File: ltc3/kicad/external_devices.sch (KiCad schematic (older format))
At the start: 68 parts, among them IC701 TLP3542, IC702 TLP3542, IC703 TLP3542, IC704 TLP3542, P701 CONN_EXT_PWR_1, P702 CONN_EXT_PWR_2, P703 CONN_EXT_PWR_3, P704 CONN_EXT_PWR_4, Q701 PMV45EN, Q702 PMV45EN, Q703 PMV45EN, Q704 PMV45EN

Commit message: LTC3: Converted hierarchical power pins to global power nodes.
This eliminates the need to manually route power from one top-level
sheet to another.
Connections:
- net VCC_12V renamed +12V
- net VCC_5V renamed +5V
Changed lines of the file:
@@
 LIBS:switches
 LIBS:CD74HC14
+LIBS:power_nodes
 LIBS:Launch_Tower_Computer_III-cache
 EELAYER 25 0
@@
 $Descr B 17000 11000
 encoding utf-8
-Sheet 6 7
+Sheet 5 7
 Title "LTC3 External Device Power"
 Date "2015-11-20"
@@
 	1    0    0    -1
 $EndComp
-Text HLabel 2650 1350 1    60   Input ~ 0
-VCC_12V
 $Comp
 L THERMISTOR PTC701
@@
 Wire Wire Line
 	1150 3000 1150 2850
-Text HLabel 1600 1600 1    60   Input ~ 0
-VCC_5V
 Wire Wire Line
 	2650 1350 2650 1550
@@
 	1    0    0    -1
 $EndComp
-Text HLabel 6850 1250 1    60   Input ~ 0
-VCC_12V
 $Comp
 L THERMISTOR PTC702
@@
 Wire Wire Line
 	5350 2900 5350 2750
-Text HLabel 5800 1500 1    60   Input ~ 0
-VCC_5V
 Wire Wire Line
 	6850 1250 6850 1450
@@
 	1    0    0    -1
 $EndComp
-Text HLabel 11050 1100 1    60   Input ~ 0
-VCC_12V
 $Comp
 L THERMISTOR PTC703
@@
 Wire Wire Line
 	9550 2750 9550 2600
-Text HLabel 10000 1350 1    60   Input ~ 0
-VCC_5V
 Wire Wire Line
 	11050 1100 11050 1300
@@
 	1    0    0    -1
 $EndComp
-Text HLabel 15250 1150 1    60   Input ~ 0
-VCC_12V
 $Comp
 L THERMISTOR PTC704
@@
 Wire Wire Line
 	13750 2800 13750 2650
-Text HLabel 14200 1400 1    60   Input ~ 0
-VCC_5V
 Wire Wire Line
 	15250 1150 15250 1350
@@
 	1    0    0    -1
 $EndComp
-Text HLabel 2150 5450 1    60   Input ~ 0
-VCC_5V
 $Comp
 L JUMPER3 JP?
@@
 	1    0    0    -1
 $EndComp
-Text HLabel 6350 5450 1    60   Input ~ 0
-VCC_5V
 $Comp
 L JUMPER3 JP?
@@
 	1    0    0    -1
 $EndComp
-Text HLabel 10550 5450 1    60   Input ~ 0
-VCC_5V
 $Comp
 L JUMPER3 JP?
@@
 	1    0    0    -1
 $EndComp
-Text HLabel 14750 5450 1    60   Input ~ 0
-VCC_5V
 $Comp
 L JUMPER3 JP?
@@
 	1    0    0    -1
 $EndComp
+$Comp
+L +5V #PWR?
+U 1 1 56544A2B
+P 1600 1600
+F 0 "#PWR?" H 1600 1450 50  0001 C CNN
+F 1 "+5V" H 1600 1740 50  0000 C CNN
+F 2 "" H 1600 1600 60  0000 C CNN
+F 3 "" H 1600 1600 60  0000 C CNN
+	1    1600 1600
+	1    0    0    -1
+$EndComp
+$Comp
+L +12V #PWR?
+U 1 1 56544B0B
+P 2650 1350
+F 0 "#PWR?" H 2650 1200 50  0001 C CNN
+F 1 "+12V" H 2650 1490 50  0000 C CNN
+F 2 "" H 2650 1350 60  0000 C CNN
+F 3 "" H 2650 1350 60  0000 C CNN
+	1    2650 1350
+	1    0    0    -1
+$EndComp
+$Comp
+L +5V #PWR?
+U 1 1 56545C1F
+P 5800 1500
+F 0 "#PWR?" H 5800 1350 50  0001 C CNN
+F 1 "+5V" H 5800 1640 50  0000 C CNN
+F 2 "" H 5800 1500 60  0000 C CNN
+F 3 "" H 5800 1500 60  0000 C CNN
+	1    5800 1500
+	1    0    0    -1
+$EndComp
+$Comp
+L +12V #PWR?
+U 1 1 56545CFF
+P 6850 1250
+F 0 "#PWR?" H 6850 1100 50  0001 C CNN
+F 1 "+12V" H 6850 1390 50  0000 C CNN
+F 2 "" H 6850 1250 60  0000 C CNN
+F 3 "" H 6850 1250 60  0000 C CNN
+	1    6850 1250
+	1    0    0    -1
+$EndComp
+$Comp
+L +5V #PWR?
+U 1 1 56546FEF
+P 10000 1350
+F 0 "#PWR?" H 10000 1200 50  0001 C CNN
+F 1 "+5V" H 10000 1490 50  0000 C CNN
+F 2 "" H 10000 1350 60  0000 C CNN
+F 3 "" H 10000 1350 60  0000 C CNN
+	1    10000 1350
+	1    0    0    -1
+$EndComp
+$Comp
+L +12V #PWR?
+U 1 1 565470CF
+P 11050 1100
+F 0 "#PWR?" H 11050 950 50  0001 C CNN
+F 1 "+12V" H 11050 1240 50  0000 C CNN
+F 2 "" H 11050 1100 60  0000 C CNN
+F 3 "" H 11050 1100 60  0000 C CNN
+	1    11050 1100
+	1    0    0    -1
+$EndComp
+$Comp
+L +5V #PWR?
+U 1 1 56547DE7
+P 14200 1400
+F 0 "#PWR?" H 14200 1250 50  0001 C CNN
+F 1 "+5V" H 14200 1540 50  0000 C CNN
+F 2 "" H 14200 1400 60  0000 C CNN
+F 3 "" H 14200 1400 60  0000 C CNN
+	1    14200 1400
+	1    0    0    -1
+$EndComp
+$Comp
+L +12V #PWR?
+U 1 1 56547EC7
+P 15250 1150
+F 0 "#PWR?" H 15250 1000 50  0001 C CNN
+F 1 "+12V" H 15250 1290 50  0000 C CNN
+F 2 "" H 15250 1150 60  0000 C CNN
+F 3 "" H 15250 1150 60  0000 C CNN
+	1    15250 1150
+	1    0    0    -1
+$EndComp
+$Comp
+L +5V #PWR?
+U 1 1 565495B3
+P 14750 5450
+F 0 "#PWR?" H 14750 5300 50  0001 C CNN
+F 1 "+5V" H 14750 5590 50  0000 C CNN
+F 2 "" H 14750 5450 60  0000 C CNN
+F 3 "" H 14750 5450 60  0000 C CNN
+	1    14750 5450
+	1    0    0    -1
+$EndComp
+$Comp
+L +5V #PWR?
+U 1 1 5654A85F
+P 10550 5450
+F 0 "#PWR?" H 10550 5300 50  0001 C CNN
+F 1 "+5V" H 10550 5590 50  0000 C CNN
+F 2 "" H 10550 5450 60  0000 C CNN
+F 3 "" H 10550 5450 60  0000 C CNN
+	1    10550 5450
+	1    0    0    -1
+$EndComp
+$Comp
+L +5V #PWR?
+U 1 1 5654BEC3
+P 6350 5450
+F 0 "#PWR?" H 6350 5300 50  0001 C CNN
+F 1 "+5V" H 6350 5590 50  0000 C CNN
+F 2 "" H 6350 5450 60  0000 C CNN
+F 3 "" H 6350 5450 60  0000 C CNN
+	1    6350 5450
+	1    0    0    -1
+$EndComp
+$Comp
+L +5V #PWR?
+U 1 1 5654DBCB
+P 2150 5450
+F 0 "#PWR?" H 2150 5300 50  0001 C CNN
+F 1 "+5V" H 2150 5590 50  0000 C CNN
+F 2 "" H 2150 5450 60  0000 C CNN
+F 3 "" H 2150 5450 60  0000 C CNN
+	1    2150 5450
+	1    0    0    -1
+$EndComp

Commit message: LTC3: Misc. edits to rocket umbilical schematic.
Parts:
- gave numbers to parts that had none: 36
- renumbered C703 to C501, C704 to C502, C702 to C503, C701 to C504, IC703 to IC501, IC704 to IC502, IC702 to IC503, IC701 to IC504, P703 to P501, P704 to P502, P702 to P503, P701 to P504, PTC703 to PTC501, PTC704 to PTC502, PTC702 to PTC503, PTC701 to PTC504, Q703 to Q501, Q704 to Q502, Q702 to Q503, Q701 to Q504, R707 to R501, R708 to R502, R702 to R503, R701 to R504, R709 to R505, R710 to R506, R704 to R507, R703 to R508, R711 to R509, R712 to R510, R706 to R511, R705 to R512

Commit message: LTC3: Cleaned up external devices schematic; other minor cosmetic edits.
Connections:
- net GPIO_EXT_PWR_1 renamed EXT_PWR_EN_1
- net GPIO_EXT_PWR_2 renamed EXT_PWR_EN_2
- net GPIO_EXT_PWR_3 renamed EXT_PWR_EN_3
- net GPIO_EXT_PWR_4 renamed EXT_PWR_EN_4
- net GPIO_EXT_TRIG_1 renamed EXT_TRIG_EN_1
- net GPIO_EXT_TRIG_2 renamed EXT_TRIG_EN_2
- net GPIO_EXT_TRIG_3 renamed EXT_TRIG_EN_3
- net GPIO_EXT_TRIG_4 renamed EXT_TRIG_EN_4
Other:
- note added: "External Device Power"
- note added: "External Device Triggers"
- note added: "TODO:\n* Determine values for bleeder resistor\n and filter capacitor on each output connector.\n* Pick new PolyFuses, 0.5-1.0A max."
- note removed: "TODO:\n* Determine values for bleeder resistor\n and filter capacitor on each output connector.\n* Pick new PolyFuses, 0.5-1.0A max.\n* Pick shorter names for hierarchical pins.\n* Prettify!"
- moved on the sheet: C501, C502, C503, C504, C505, C506, C507, C508, IC501, IC502, IC503, IC504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

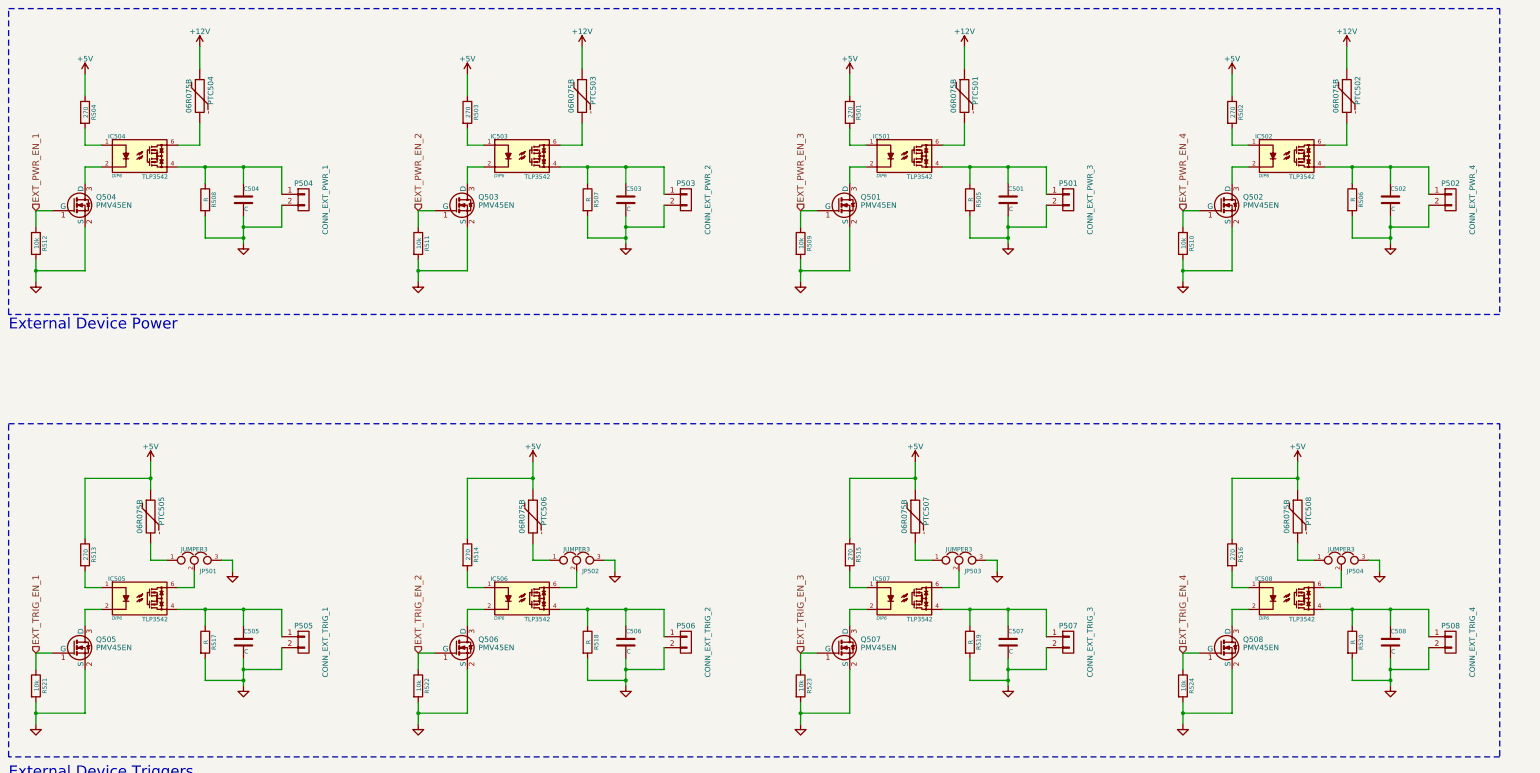
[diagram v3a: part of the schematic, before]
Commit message: LTC3: Reordered schematic sub-sheets; updated PDF export of schematic.
KiCad has an odd habit of ordering a schematic's sub-sheets without
notice.
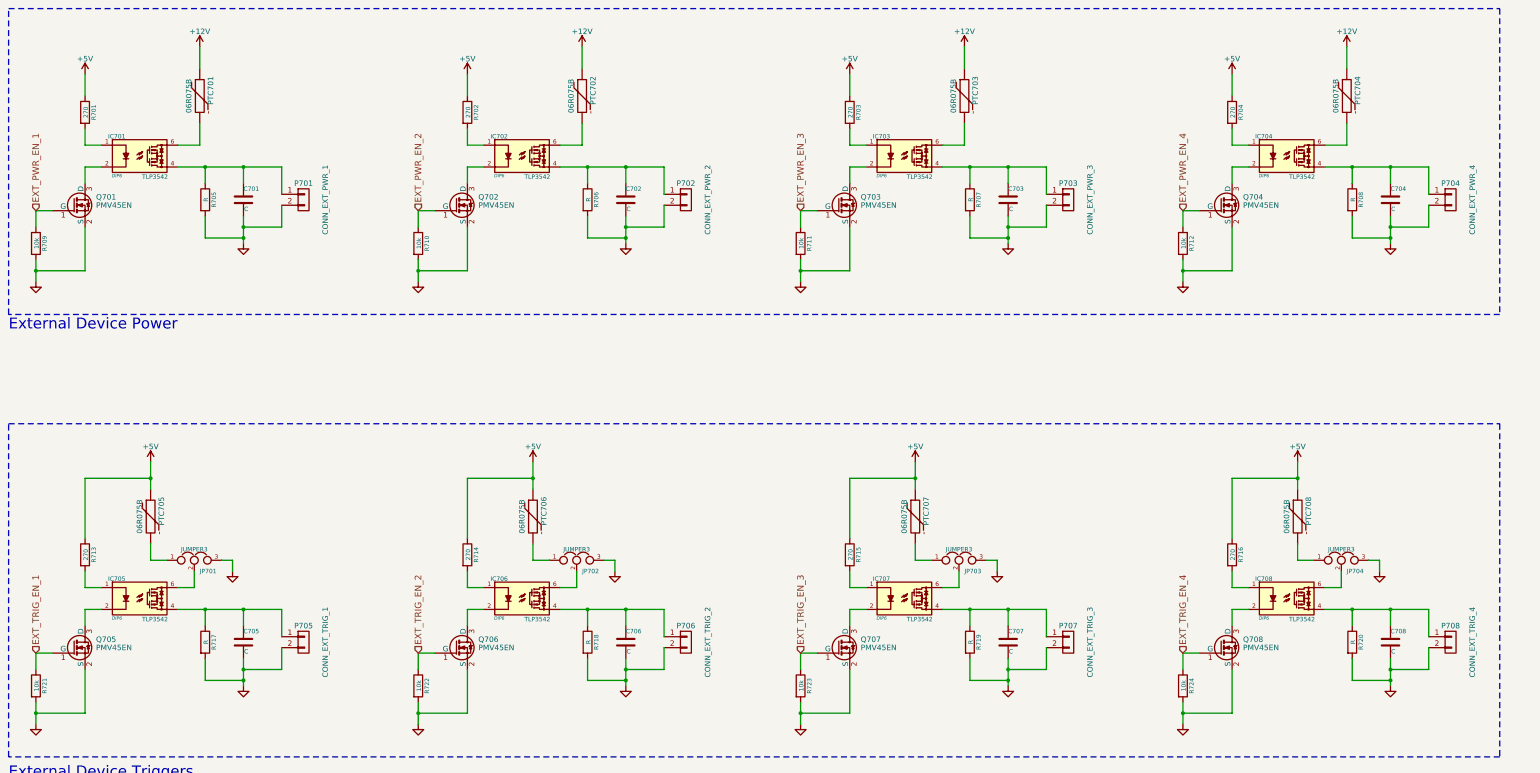
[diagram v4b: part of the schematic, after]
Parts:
- renumbered C504 to C701, C503 to C702, C501 to C703, C502 to C704, C505 to C705, C506 to C706, C507 to C707, C508 to C708, IC504 to IC701, IC503 to IC702, IC501 to IC703, IC502 to IC704, IC505 to IC705, IC506 to IC706, IC507 to IC707, IC508 to IC708, JP501 to JP701, JP502 to JP702, JP503 to JP703, JP504 to JP704, P504 to P701, P503 to P702, P501 to P703, P502 to P704, P505 to P705, P506 to P706, P507 to P707, P508 to P708, PTC504 to PTC701, PTC503 to PTC702, PTC501 to PTC703, PTC502 to PTC704, PTC505 to PTC705, PTC506 to PTC706, PTC507 to PTC707, PTC508 to PTC708, Q504 to Q701, Q503 to Q702, Q501 to Q703, Q502 to Q704, Q505 to Q705, Q506 to Q706, Q507 to Q707, Q508 to Q708, R504 to R701, R503 to R702, R501 to R703, R502 to R704, R508 to R705, R507 to R706, R505 to R707, R506 to R708, R512 to R709, R511 to R710, R509 to R711, R510 to R712, R513 to R713, R514 to R714, R515 to R715, R516 to R716, R517 to R717, R518 to R718, R519 to R719, R520 to R720, R521 to R721, R522 to R722, R523 to R723, R524 to R724

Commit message: LTC3: Cleaned up I2C devices.
Gave each power sub-circuit its own LTC299x sensor.  Charger and
battery pack circuits each get an LTC2990 (quad); DC-DC converter
circuit gets an LTC2991 (octal).

Separate sensor ICs for each sub-circuit allows the chip to be as
close to its sense resistors as possible (and makes for a cleaner
schematic).
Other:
- moved on the sheet: C705, C706, C707, C708, IC705, IC706, IC707, IC708, JP701, JP702, JP703, JP704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

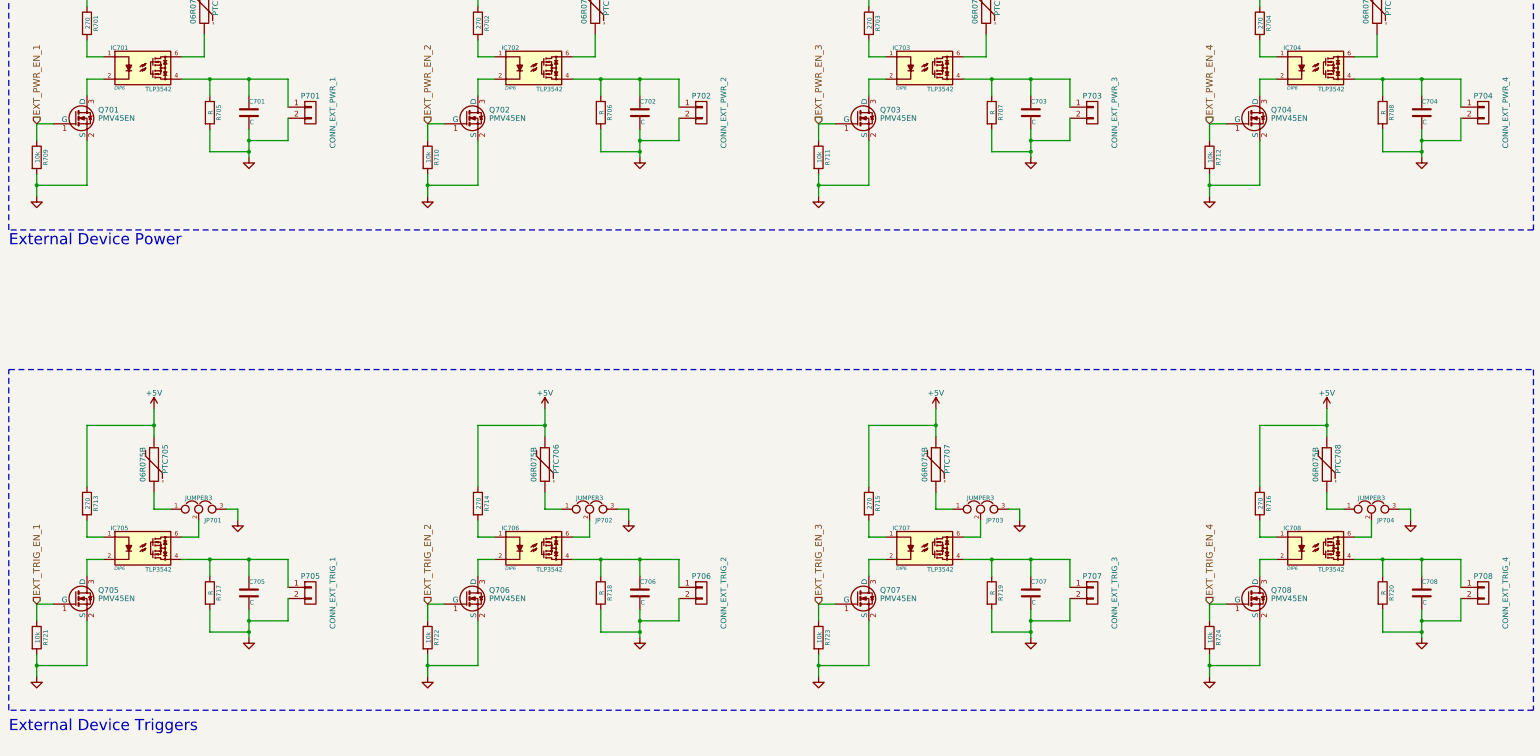
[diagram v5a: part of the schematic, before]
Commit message: LTC3: Cosmetic edit to external devices sheet.
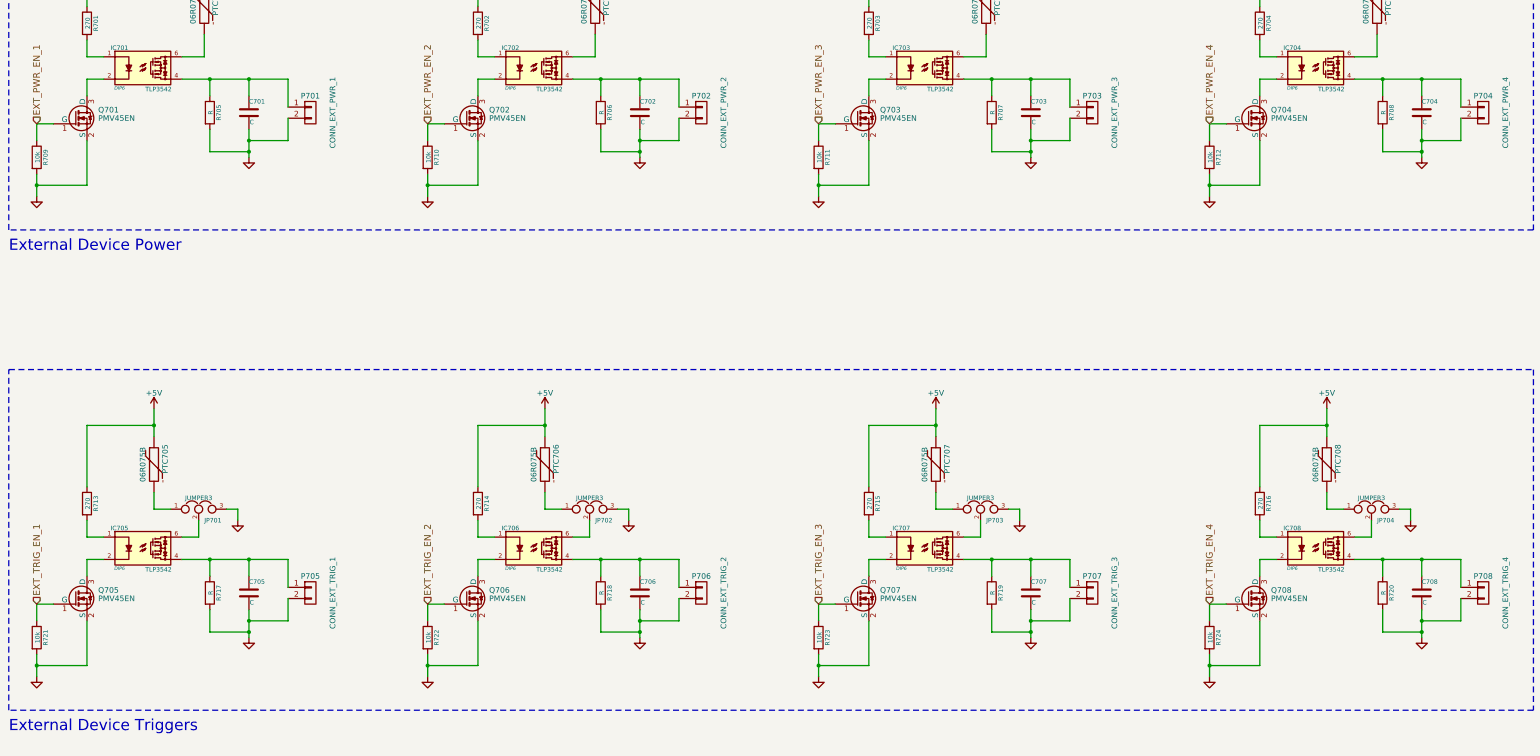
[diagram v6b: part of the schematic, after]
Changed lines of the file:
@@
 	2400 3350 2400 3750
 Wire Wire Line
-	1950 3650 1950 3750
-Wire Wire Line
-	1950 3750 1950 3850
+	1950 3650 1950 3850
 Wire Wire Line
 	3850 2800 3850 2950
@@
 	3500 3450 3500 3250
 Wire Wire Line
-	3850 3250 3850 3350
-Wire Wire Line
-	3850 3350 3850 3450
-Wire Wire Line
-	3850 3450 3850 3500
+	3850 3250 3850 3500
 Wire Wire Line
 	2400 2800 2400 2950
@@
 	3500 2800 3500 2950
 Wire Wire Line
-	3250 2800 3500 2800
-Wire Wire Line
-	3500 2800 3850 2800
-Wire Wire Line
-	3850 2800 4200 2800
+	3250 2800 4200 2800
 Wire Wire Line
 	2550 2800 2400 2800
@@
 	5900 3350 5900 3750
 Wire Wire Line
-	5450 3650 5450 3750
-Wire Wire Line
-	5450 3750 5450 3850
+	5450 3650 5450 3850
 Wire Wire Line
 	7350 2800 7350 2950
@@
 	7000 3450 7000 3250
 Wire Wire Line
-	7350 3250 7350 3350
-Wire Wire Line
-	7350 3350 7350 3450
-Wire Wire Line
-	7350 3450 7350 3500
+	7350 3250 7350 3500
 Wire Wire Line
 	5900 2800 5900 2950
@@
 	7000 2800 7000 2950
 Wire Wire Line
-	6750 2800 7000 2800
-Wire Wire Line
-	7000 2800 7350 2800
-Wire Wire Line
-	7350 2800 7700 2800
+	6750 2800 7700 2800
 Wire Wire Line
 	6050 2800 5900 2800
@@
 	9400 3350 9400 3750
 Wire Wire Line
-	8950 3650 8950 3750
-Wire Wire Line
-	8950 3750 8950 3850
+	8950 3650 8950 3850
 Wire Wire Line
 	10850 2800 10850 2950
@@
 	10500 3450 10500 3250
 Wire Wire Line
-	10850 3250 10850 3350
-Wire Wire Line
-	10850 3350 10850 3450
-Wire Wire Line
-	10850 3450 10850 3500
+	10850 3250 10850 3500
 Wire Wire Line
 	9400 2800 9400 2950
@@
 	10500 2800 10500 2950
 Wire Wire Line
-	10250 2800 10500 2800
-Wire Wire Line
-	10500 2800 10850 2800
-Wire Wire Line
-	10850 2800 11200 2800
+	10250 2800 11200 2800
 Wire Wire Line
 	9550 2800 9400 2800
@@
 	12900 3350 12900 3750
 Wire Wire Line
-	12450 3650 12450 3750
-Wire Wire Line
-	12450 3750 12450 3850
+	12450 3650 12450 3850
 Wire Wire Line
 	14350 2800 14350 2950
@@
 	14000 3450 14000 3250
 Wire Wire Line
-	14350 3250 14350 3350
-Wire Wire Line
-	14350 3350 14350 3450
-Wire Wire Line
-	14350 3450 14350 3500
+	14350 3250 14350 3500
 Wire Wire Line
 	12900 2800 12900 2950
@@
 	14000 2800 14000 2950
 Wire Wire Line
-	13750 2800 14000 2800
-Wire Wire Line
-	14000 2800 14350 2800
-Wire Wire Line
-	14350 2800 14700 2800
+	13750 2800 14700 2800
 Wire Wire Line
 	13050 2800 12900 2800
@@
 	3400 6900 3250 6900
 Wire Wire Line
-	3000 5750 3000 5900
-Wire Wire Line
-	3000 5900 3000 6000
+	3000 5750 3000 6000
 Wire Wire Line
 	2550 7100 2400 7100
@@
 	3400 6750 3400 6900
 Wire Wire Line
-	3250 7100 3500 7100
-Wire Wire Line
-	3500 7100 3850 7100
-Wire Wire Line
-	3850 7100 4200 7100
+	3250 7100 4200 7100
 Wire Wire Line
 	3500 7100 3500 7250
@@
 	2400 7100 2400 7250
 Wire Wire Line
-	3850 7550 3850 7650
-Wire Wire Line
-	3850 7650 3850 7750
-Wire Wire Line
-	3850 7750 3850 7800
+	3850 7550 3850 7800
 Wire Wire Line
 	3500 7550 3500 7750
@@
 	3850 7250 3850 7100
 Wire Wire Line
-	1950 7950 1950 8050
-Wire Wire Line
-	1950 8050 1950 8150
+	1950 7950 1950 8150
 Wire Wire Line
 	2400 7650 2400 8050
@@
 	6900 6900 6750 6900
 Wire Wire Line
-	6500 5750 6500 5900
-Wire Wire Line
-	6500 5900 6500 6000
+	6500 5750 6500 6000
 Wire Wire Line
 	6050 7100 5900 7100
@@
 	6900 6750 6900 6900
 Wire Wire Line
-	6750 7100 7000 7100
-Wire Wire Line
-	7000 7100 7350 7100
-Wire Wire Line
-	7350 7100 7700 7100
+	6750 7100 7700 7100
 Wire Wire Line
 	7000 7100 7000 7250
@@
 	5900 7100 5900 7250
 Wire Wire Line
-	7350 7550 7350 7650
-Wire Wire Line
-	7350 7650 7350 7750
-Wire Wire Line
-	7350 7750 7350 7800
+	7350 7550 7350 7800
 Wire Wire Line
 	7000 7550 7000 7750
@@
 	7350 7250 7350 7100
 Wire Wire Line
-	5450 7950 5450 8050
-Wire Wire Line
-	5450 8050 5450 8150
+	5450 7950 5450 8150
 Wire Wire Line
 	5900 7650 5900 8050
@@
 	10400 6900 10250 6900
 Wire Wire Line
-	10000 5750 10000 5900
-Wire Wire Line
-	10000 5900 10000 6000
+	10000 5750 10000 6000
 Wire Wire Line
 	9550 7100 9400 7100
@@
 	10400 6750 10400 6900
 Wire Wire Line
-	10250 7100 10500 7100
-Wire Wire Line
-	10500 7100 10850 7100
-Wire Wire Line
-	10850 7100 11200 7100
+	10250 7100 11200 7100
 Wire Wire Line
 	10500 7100 10500 7250
@@
 	9400 7100 9400 7250
 Wire Wire Line
-	10850 7550 10850 7650
-Wire Wire Line
-	10850 7650 10850 7750
-Wire Wire Line
-	10850 7750 10850 7800
+	10850 7550 10850 7800
 Wire Wire Line
 	10500 7550 10500 7750
@@
 	10850 7250 10850 7100
 Wire Wire Line
-	8950 7950 8950 8050
-Wire Wire Line
-	8950 8050 8950 8150
+	8950 7950 8950 8150
 Wire Wire Line
 	9400 7650 9400 8050
@@
 	13900 6900 13750 6900
 Wire Wire Line
-	13500 5750 13500 5900
-Wire Wire Line
-	13500 5900 13500 6000
+	13500 5750 13500 6000
 Wire Wire Line
 	13050 7100 12900 7100
@@
 	13900 6750 13900 6900
 Wire Wire Line
-	13750 7100 14000 7100
-Wire Wire Line
-	14000 7100 14350 7100
-Wire Wire Line
-	14350 7100 14700 7100
+	13750 7100 14700 7100
 Wire Wire Line
 	14000 7100 14000 7250
@@
 	12900 7100 12900 7250
 Wire Wire Line
-	14350 7550 14350 7650
-Wire Wire Line
-	14350 7650 14350 7750
-Wire Wire Line
-	14350 7750 14350 7800
+	14350 7550 14350 7800
 Wire Wire Line
 	14000 7550 14000 7750
@@
 	14350 7250 14350 7100
 Wire Wire Line
-	12450 7950 12450 8050
-Wire Wire Line
-	12450 8050 12450 8150
+	12450 7950 12450 8150
 Wire Wire Line
 	12900 7650 12900 8050
@@
 Wire Notes Line
 	1700 4150 1700 1350
-Text Notes 1700 4300 0    100  ~ 0
+Text Notes 1700 4350 0    100  ~ 0
 External Device Power
 Wire Wire Line
